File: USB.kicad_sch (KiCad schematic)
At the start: 7 parts

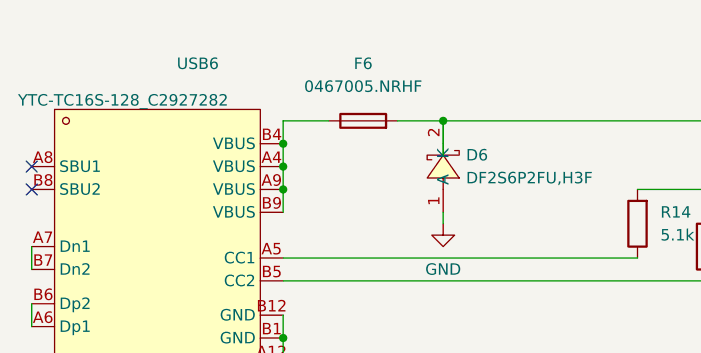
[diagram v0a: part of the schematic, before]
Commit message: sarted routing of the usb circuitry, almost finished it
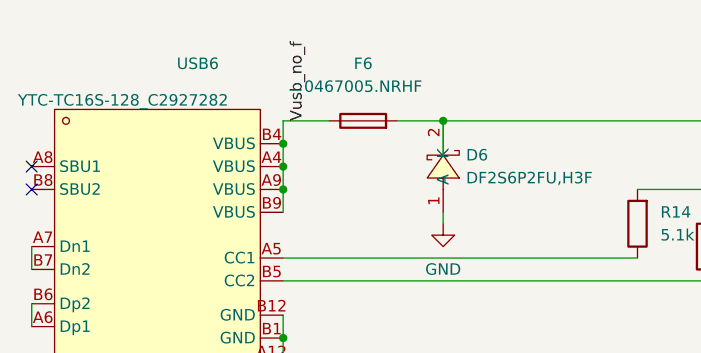
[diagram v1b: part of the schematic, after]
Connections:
- net Vusb_no_f: now reaches F6.1, USB6.A4 (VBUS), USB6.A9 (VBUS), USB6.B4 (VBUS), USB6.B9 (VBUS)
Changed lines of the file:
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@@
+		)
+	)
+	(label "Vusb_no_f"
+		(at 148.59 57.15 90)
+		(effects
+			(font
+				(size 1.27 1.27)
+			)
+			(justify left bottom)
 		)
 	)
